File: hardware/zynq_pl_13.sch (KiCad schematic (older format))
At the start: 1 part, among them U1 xc7z030sbg485

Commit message: Added Power/Protection Circuit
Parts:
- renumbered U1 to U201
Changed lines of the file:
@@
 $EndDescr
 $Comp
-L xc7z030sbg485 U1
+L xc7z030sbg485 U201
 U 2 1 596E7737
 P 7200 1200
-F 0 "U1" H 7400 1450 60  0000 L CNN
+F 0 "U201" H 7400 1450 60  0000 L CNN
 F 1 "xc7z030sbg485" H 7400 1350 60  0000 L CNN
 F 2 "footprints:SBG485_22x22_19.0x19.0mm_Pitch0.8mm" H 7200 1200 60  0001 C CNN

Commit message: Length matched DDR3 Memory again.
Forgot to keep enough space between the traces and between the meander waves.

Also, I switched to Kicad 5.0 RC2.

Swaped a few ddr signals.
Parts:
- U201: symbol xc7z030sbg485 -> xilinx_zynq_clg485:xc7z030sbg485
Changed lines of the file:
@@
-EESchema Schematic File Version 2
-LIBS:zynq_board-rescue
-LIBS:power
-LIBS:device
-LIBS:transistors
-LIBS:conn
-LIBS:linear
-LIBS:regul
-LIBS:74xx
-LIBS:cmos4000
-LIBS:adc-dac
-LIBS:memory
-LIBS:xilinx
-LIBS:microcontrollers
-LIBS:dsp
-LIBS:microchip
-LIBS:analog_switches
-LIBS:motorola
-LIBS:texas
-LIBS:intel
-LIBS:audio
-LIBS:interface
-LIBS:digital-audio
-LIBS:philips
-LIBS:display
-LIBS:cypress
-LIBS:siliconi
-LIBS:opto
-LIBS:atmel
-LIBS:contrib
-LIBS:valves
-LIBS:xilinx_zynq_clg485
-LIBS:SFP_plus
-LIBS:ael2005
-LIBS:diff_osc
-LIBS:si53340
-LIBS:usb3320
-LIBS:nx5p3090
-LIBS:smp1255putg
-LIBS:osc
-LIBS:ddr
-LIBS:misc
-LIBS:tlk10031
-LIBS:lshm-150-xxx-x-dv-a-s
-LIBS:sn74axc8t245
-LIBS:sn74lvc2t45
-LIBS:dmf05lcflp
-LIBS:bss138ps
-LIBS:max14854
-LIBS:switches
-LIBS:ft234xd
-LIBS:sn74lv1t126
-LIBS:emif06-msd02n16
-LIBS:cat24c02tdi-gt3
-LIBS:power_symbols
-LIBS:ti_power_modules
-LIBS:mdr20
-LIBS:dm3cs
-LIBS:lsf0102
-LIBS:dmp3056l
+EESchema Schematic File Version 4
 LIBS:zynq_board-cache
-EELAYER 25 0
+EELAYER 26 0
 EELAYER END
 $Descr A4 11693 8268
@@
 $EndDescr
 $Comp
-L xc7z030sbg485 U201
+L xilinx_zynq_clg485:xc7z030sbg485 U201
 U 2 1 596E7737
 P 7200 1200

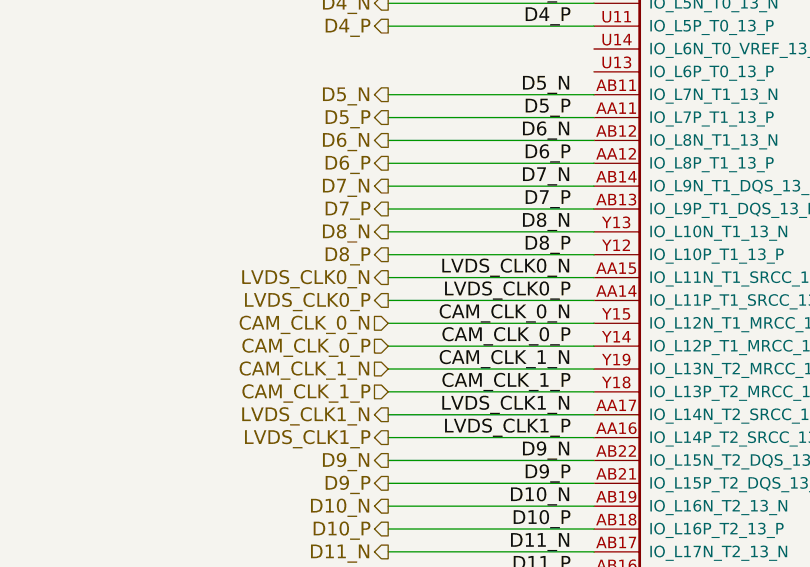
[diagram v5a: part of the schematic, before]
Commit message: PS Clock, Reset Button, Cam Levelshifters and big 1.0 V Cap placed.
Improved some Footprints and library Symbols.

Also though about Chassis Ground.
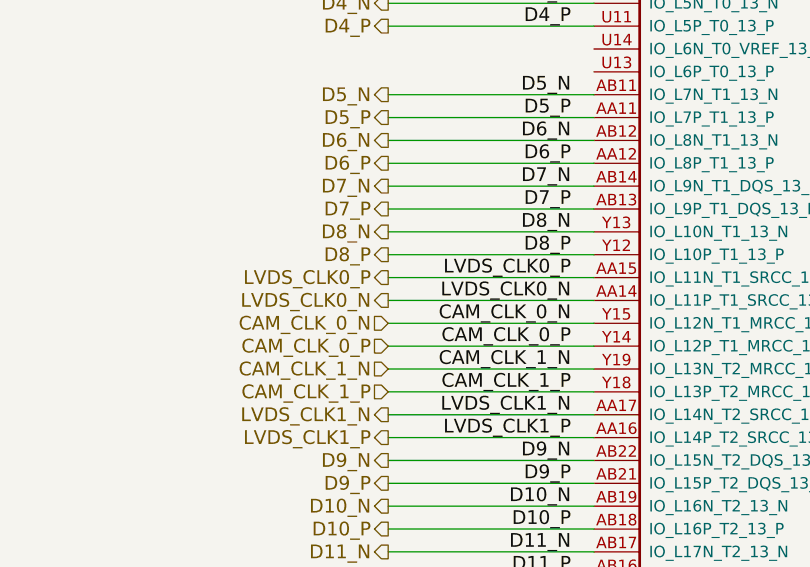
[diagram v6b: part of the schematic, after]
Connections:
- net LVDS_CLK0_N: now also U201.AA14 (IO_L11P_T1_SRCC_13_P); no longer U201.AA15 (IO_L11N_T1_SRCC_13_N)
- net LVDS_CLK0_P: now also U201.AA15 (IO_L11N_T1_SRCC_13_N); no longer U201.AA14 (IO_L11P_T1_SRCC_13_P)
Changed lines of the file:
@@
 Wire Wire Line
 	6300 3300 7200 3300
+Text HLabel 6300 3500 0    60   Output ~ 0
+LVDS_CLK0_N
 Text HLabel 6300 3400 0    60   Output ~ 0
-LVDS_CLK0_N
-Text HLabel 6300 3500 0    60   Output ~ 0
 LVDS_CLK0_P
 Text HLabel 6300 4000 0    60   Output ~ 0
@@
 LVDS_CLK1_P
 Wire Wire Line
-	6300 3400 7200 3400
+	6300 3500 7200 3500
 Wire Wire Line
-	7200 3500 6300 3500
+	7200 3400 6300 3400
 Wire Wire Line
 	6300 4000 7200 4000
 Wire Wire Line
 	7200 4100 6300 4100
+Text Label 7100 3500 2    60   ~ 0
+LVDS_CLK0_N
 Text Label 7100 3400 2    60   ~ 0
-LVDS_CLK0_N
-Text Label 7100 3500 2    60   ~ 0
 LVDS_CLK0_P
 Text Label 7100 3600 2    60   ~ 0

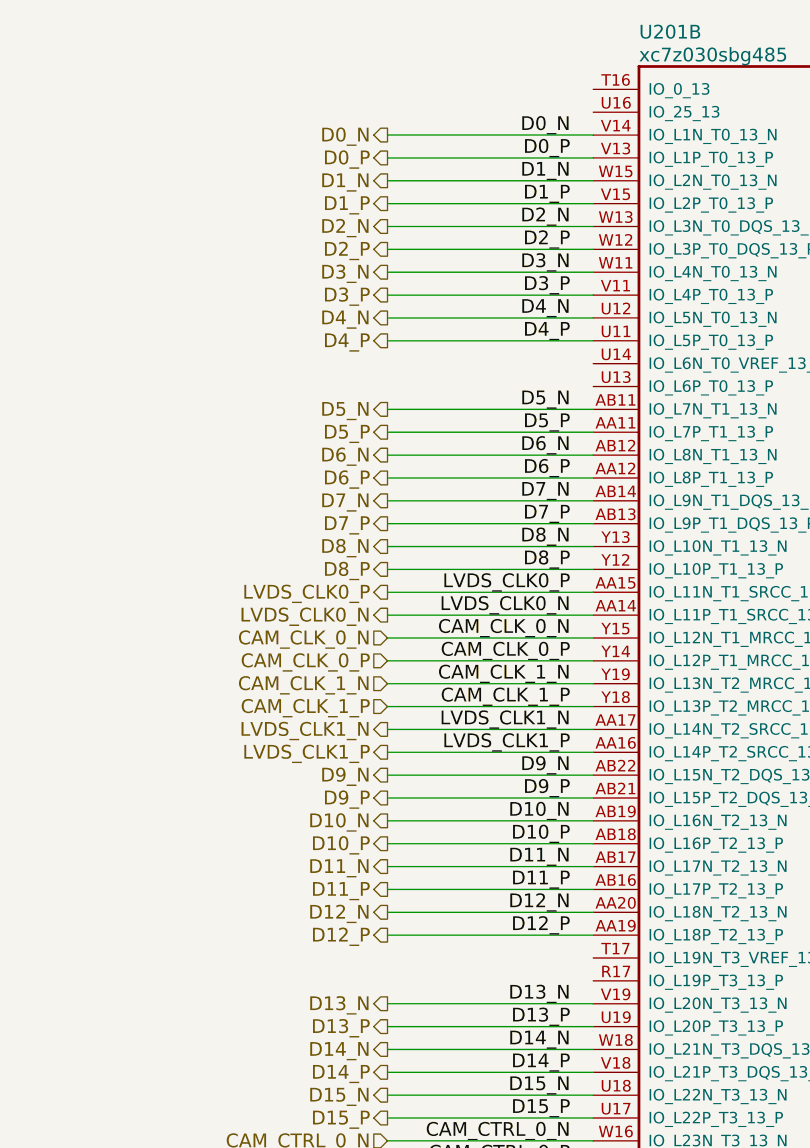
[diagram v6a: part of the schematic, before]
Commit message: WIP: routing the HF Part of the Camera Connector. I have to move the clock away from the left border.
TODO: Fix DDR3 RAM.
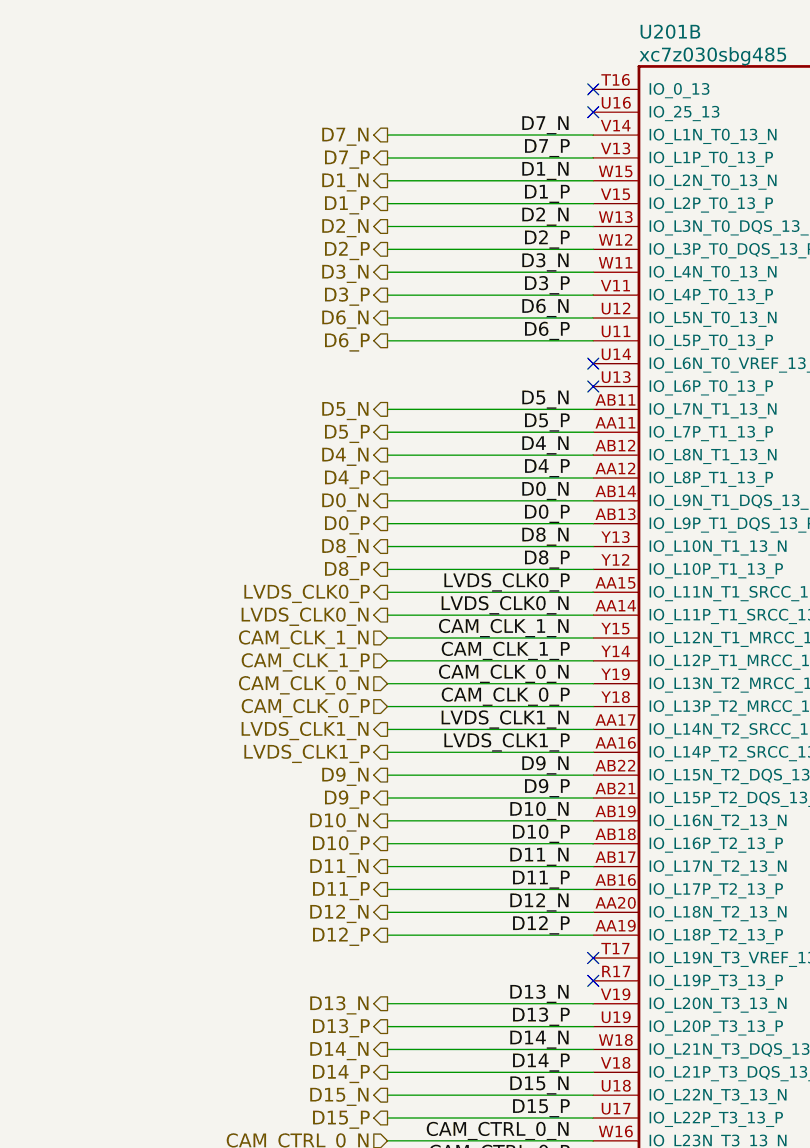
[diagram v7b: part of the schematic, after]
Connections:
- net CAM_CLK_0_N: now also U201.Y19 (IO_L13N_T2_MRCC_13_N); no longer U201.Y15 (IO_L12N_T1_MRCC_13_N)
- net CAM_CLK_0_P: now also U201.Y18 (IO_L13P_T2_MRCC_13_P); no longer U201.Y14 (IO_L12P_T1_MRCC_13_P)
- net CAM_CLK_1_N: now also U201.Y15 (IO_L12N_T1_MRCC_13_N); no longer U201.Y19 (IO_L13N_T2_MRCC_13_N)
- net CAM_CLK_1_P: now also U201.Y14 (IO_L12P_T1_MRCC_13_P); no longer U201.Y18 (IO_L13P_T2_MRCC_13_P)
- net D0_N: now also U201.AB14 (IO_L9N_T1_DQS_13_N); no longer U201.V14 (IO_L1N_T0_13_N)
- net D0_P: now also U201.AB13 (IO_L9P_T1_DQS_13_P); no longer U201.V13 (IO_L1P_T0_13_P)
- net D4_N: now also U201.AB12 (IO_L8N_T1_13_N); no longer U201.U12 (IO_L5N_T0_13_N)
- net D4_P: now also U201.AA12 (IO_L8P_T1_13_P); no longer U201.U11 (IO_L5P_T0_13_P)
- net D6_N: now also U201.U12 (IO_L5N_T0_13_N); no longer U201.AB12 (IO_L8N_T1_13_N)
- net D6_P: now also U201.U11 (IO_L5P_T0_13_P); no longer U201.AA12 (IO_L8P_T1_13_P)
- net D7_N: now also U201.V14 (IO_L1N_T0_13_N); no longer U201.AB14 (IO_L9N_T1_DQS_13_N)
- net D7_P: now also U201.V13 (IO_L1P_T0_13_P); no longer U201.AB13 (IO_L9P_T1_DQS_13_P)
- no-connect marks 0 -> 6
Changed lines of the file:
@@
 Text HLabel 6300 5800 0    60   Input ~ 0
 CAM_CTRL_0_N
-Text HLabel 6300 3700 0    60   Input ~ 0
+Text HLabel 6300 3900 0    60   Input ~ 0
 CAM_CLK_0_P
-Text HLabel 6300 3600 0    60   Input ~ 0
+Text HLabel 6300 3800 0    60   Input ~ 0
 CAM_CLK_0_N
 Text HLabel 6300 6100 0    60   Input ~ 0
@@
 Text HLabel 6300 6000 0    60   Input ~ 0
 CAM_CTRL_1_N
-Text HLabel 6300 3900 0    60   Input ~ 0
+Text HLabel 6300 3700 0    60   Input ~ 0
 CAM_CLK_1_P
-Text HLabel 6300 3800 0    60   Input ~ 0
+Text HLabel 6300 3600 0    60   Input ~ 0
 CAM_CLK_1_N
 Text Label 7100 5600 2    60   ~ 0
@@
 Text Label 7100 4300 2    60   ~ 0
 D9_P
-Text HLabel 6300 1400 0    60   Output ~ 0
+Text HLabel 6300 3000 0    60   Output ~ 0
 D0_N
-Text HLabel 6300 1500 0    60   Output ~ 0
+Text HLabel 6300 3100 0    60   Output ~ 0
 D0_P
 Text HLabel 6300 1600 0    60   Output ~ 0
@@
 Text HLabel 6300 2100 0    60   Output ~ 0
 D3_P
-Text HLabel 6300 2200 0    60   Output ~ 0
+Text HLabel 6300 2800 0    60   Output ~ 0
 D4_N
-Text HLabel 6300 2300 0    60   Output ~ 0
+Text HLabel 6300 2900 0    60   Output ~ 0
 D4_P
 Text HLabel 6300 2600 0    60   Output ~ 0
@@
 Text HLabel 6300 2700 0    60   Output ~ 0
 D5_P
-Text HLabel 6300 2800 0    60   Output ~ 0
+Text HLabel 6300 2200 0    60   Output ~ 0
 D6_N
-Text HLabel 6300 2900 0    60   Output ~ 0
+Text HLabel 6300 2300 0    60   Output ~ 0
 D6_P
-Text HLabel 6300 3000 0    60   Output ~ 0
+Text HLabel 6300 1400 0    60   Output ~ 0
 D7_N
-Text HLabel 6300 3100 0    60   Output ~ 0
+Text HLabel 6300 1500 0    60   Output ~ 0
 D7_P
 Text HLabel 6300 3200 0    60   Output ~ 0
@@
 Text HLabel 6300 5700 0    60   Output ~ 0
 D15_P
-Text Label 7100 1500 2    60   ~ 0
+Text Label 7100 3100 2    60   ~ 0
 D0_P
-Text Label 7100 1400 2    60   ~ 0
+Text Label 7100 3000 2    60   ~ 0
 D0_N
 Text Label 7100 1700 2    60   ~ 0
@@
 Text Label 7100 2000 2    60   ~ 0
 D3_N
-Text Label 7100 2300 2    60   ~ 0
+Text Label 7100 2900 2    60   ~ 0
 D4_P
-Text Label 7100 2200 2    60   ~ 0
+Text Label 7100 2800 2    60   ~ 0
 D4_N
 Text Label 7100 2700 2    60   ~ 0
@@
 Text Label 7100 2600 2    60   ~ 0
 D5_N
-Text Label 7100 2900 2    60   ~ 0
+Text Label 7100 2300 2    60   ~ 0
 D6_P
-Text Label 7100 2800 2    60   ~ 0
+Text Label 7100 2200 2    60   ~ 0
 D6_N
-Text Label 7100 3100 2    60   ~ 0
+Text Label 7100 1500 2    60   ~ 0
 D7_P
-Text Label 7100 3000 2    60   ~ 0
+Text Label 7100 1400 2    60   ~ 0
 D7_N
 Text Label 7100 3300 2    60   ~ 0
@@
 D8_N
 Wire Wire Line
-	6300 3600 7200 3600
+	6300 3800 7200 3800
+Wire Wire Line
+	6300 3900 7200 3900
+Wire Wire Line
+	7200 3600 6300 3600
 Wire Wire Line
 	6300 3700 7200 3700
-Wire Wire Line
-	7200 3800 6300 3800
-Wire Wire Line
-	6300 3900 7200 3900
 Wire Wire Line
 	6300 5800 7200 5800
@@
 Text Label 7100 3400 2    60   ~ 0
 LVDS_CLK0_P
+Text Label 7100 3800 2    60   ~ 0
+CAM_CLK_0_N
+Text Label 7100 3900 2    60   ~ 0
+CAM_CLK_0_P
 Text Label 7100 3600 2    60   ~ 0
-CAM_CLK_0_N
+CAM_CLK_1_N
 Text Label 7100 3700 2    60   ~ 0
-CAM_CLK_0_P
-Text Label 7100 3800 2    60   ~ 0
-CAM_CLK_1_N
-Text Label 7100 3900 2    60   ~ 0
 CAM_CLK_1_P
 Text Label 7100 4000 2    60   ~ 0
@@
 Wire Wire Line
 	6300 6200 7200 6200
+NoConn ~ 7200 1200
+NoConn ~ 7200 1300
+NoConn ~ 7200 2400
+NoConn ~ 7200 2500
+NoConn ~ 7200 5000
+NoConn ~ 7200 5100
 $EndSCHEMATC
